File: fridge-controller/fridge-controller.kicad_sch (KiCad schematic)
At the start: 11 parts, among them M1 Fan, U2 AMS1117-5.0, U3 Arduino_Pro_Mini, U4 TLP127, U5 Secop BD35F

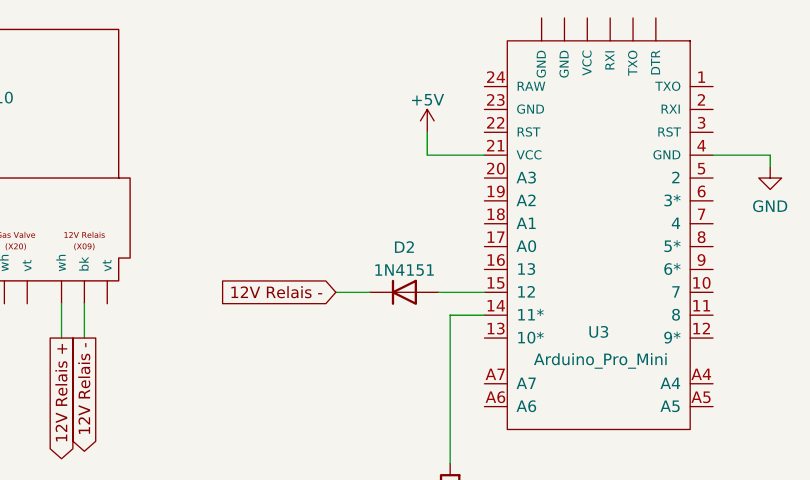
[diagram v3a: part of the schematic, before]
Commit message: Updated fridge-controller
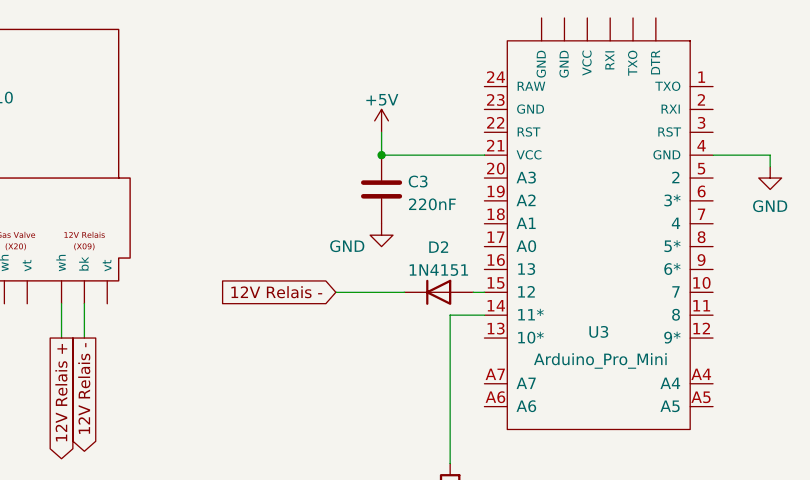
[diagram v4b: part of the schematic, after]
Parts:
- added C3: 220nF, symbol Device:C
- gave numbers to parts that had none: 1
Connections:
- net +5V: now also C3.1
- net GND: now also C3.2
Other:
- moved on the sheet: D2
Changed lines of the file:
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@@
   (title_block
     (title "Secop BD35F Compressor Speed Controller")
-    (date "2025-02-14")
+    (date "2025-02-16")
     (company "Copyright (C) 2025, Karim Hraibi")
     (comment 1 "Enables variable speed control over 5 kHz PWM signal.")
@@
   (junction (at 85.09 90.17) (diameter 0) (color 0 0 0 0)
   )
+  (junction (at 86.36 34.29) (diameter 0) (color 0 0 0 0)
+  )
   (wire (pts (xy 152.4 80.01) (xy 154.94 80.01))
     (stroke (width 0) (type default) (color 0 0 0 0))
@@
     (stroke (width 0) (type default) (color 0 0 0 0))
   )
-  (wire (pts (xy 97.79 49.53) (xy 92.71 49.53))
+  (wire (pts (xy 97.79 49.53) (xy 96.52 49.53))
     (stroke (width 0) (type default) (color 0 0 0 0))
   )
@@
     (stroke (width 0) (type default) (color 0 0 0 0))
   )
-  (wire (pts (xy 91.44 34.29) (xy 97.79 34.29))
+  (wire (pts (xy 86.36 34.29) (xy 97.79 34.29))
     (stroke (width 0) (type default) (color 0 0 0 0))
   )
@@
     (stroke (width 0) (type default) (color 0 0 0 0))
   )
-  (wire (pts (xy 85.09 49.53) (xy 81.28 49.53))
+  (wire (pts (xy 88.9 49.53) (xy 81.28 49.53))
     (stroke (width 0) (type default) (color 0 0 0 0))
   )
@@
     (stroke (width 0) (type default) (color 0 0 0 0))
   )
-  (wire (pts (xy 91.44 31.75) (xy 91.44 34.29))
+  (wire (pts (xy 86.36 31.75) (xy 86.36 34.29))
     (stroke (width 0) (type default) (color 0 0 0 0))
   )
@@
     )
   )
+  (symbol (lib_id "Device:C") (at 86.36 38.1 0) (unit 1)
+    (in_bom yes) (on_board yes)
+    (property "Reference" "C3" (id 0) (at 89.281 37.2653 0)
+      (effects (font (size 1.27 1.27)) (justify left))
+    )
+    (property "Value" "220nF" (id 1) (at 89.281 39.8022 0)
+      (effects (font (size 1.27 1.27)) (justify left))
+    )
+    (property "Footprint" "" (id 2) (at 87.3252 41.91 0)
+      (effects (font (size 1.27 1.27)) hide)
+    )
+    (property "Datasheet" "~" (id 3) (at 86.36 38.1 0)
+      (effects (font (size 1.27 1.27)) hide)
+    )
+    (pin "1")
+    (pin "2")
+  )
   (symbol (lib_id "Device:R") (at 93.98 72.39 180) (unit 1)
     (in_bom yes) (on_board yes) (fields_autoplaced)
@@
   (symbol (lib_id "power:GND") (at 100.33 87.63 0) (unit 1)
     (in_bom yes) (on_board yes) (fields_autoplaced)
-    (property "Reference" "#PWR04" (id 0) (at 100.33 93.98 0)
+    (property "Reference" "#PWR05" (id 0) (at 100.33 93.98 0)
       (effects (font (size 1.27 1.27)) hide)
     )
@@
     (pin "1")
   )
-  (symbol (lib_id "Diode:1N4151") (at 88.9 49.53 0) (unit 1)
-    (in_bom yes) (on_board yes) (fields_autoplaced)
-    (property "Reference" "D2" (id 0) (at 88.9 44.5602 0))
-    (property "Value" "1N4151" (id 1) (at 88.9 47.0971 0))
-    (property "Footprint" "Diode_THT:D_DO-35_SOD27_P7.62mm_Horizontal" (id 2) (at 88.9 53.975 0)
-      (effects (font (size 1.27 1.27)) hide)
-    )
-    (property "Datasheet" "http://www.microsemi.com/document-portal/doc_view/11580-lds-0239" (id 3) (at 88.9 49.53 0)
+  (symbol (lib_id "Diode:1N4151") (at 92.71 49.53 0) (unit 1)
+    (in_bom yes) (on_board yes) (fields_autoplaced)
+    (property "Reference" "D2" (id 0) (at 92.71 44.5602 0))
+    (property "Value" "1N4151" (id 1) (at 92.71 47.0971 0))
+    (property "Footprint" "Diode_THT:D_DO-35_SOD27_P7.62mm_Horizontal" (id 2) (at 92.71 53.975 0)
+      (effects (font (size 1.27 1.27)) hide)
+    )
+    (property "Datasheet" "http://www.microsemi.com/document-portal/doc_view/11580-lds-0239" (id 3) (at 92.71 49.53 0)
       (effects (font (size 1.27 1.27)) hide)
     )
@@
   (symbol (lib_id "power:GND") (at 129.54 35.56 0) (unit 1)
     (in_bom yes) (on_board yes) (fields_autoplaced)
-    (property "Reference" "#PWR05" (id 0) (at 129.54 41.91 0)
+    (property "Reference" "#PWR06" (id 0) (at 129.54 41.91 0)
       (effects (font (size 1.27 1.27)) hide)
     )
@@
     (pin "1")
   )
-  (symbol (lib_id "power:+5V") (at 91.44 31.75 0) (unit 1)
-    (in_bom yes) (on_board yes) (fields_autoplaced)
-    (property "Reference" "#PWR03" (id 0) (at 91.44 35.56 0)
-      (effects (font (size 1.27 1.27)) hide)
-    )
-    (property "Value" "+5V" (id 1) (at 91.44 28.1742 0))
-    (property "Footprint" "" (id 2) (at 91.44 31.75 0)
-      (effects (font (size 1.27 1.27)) hide)
-    )
-    (property "Datasheet" "" (id 3) (at 91.44 31.75 0)
+  (symbol (lib_id "power:+5V") (at 86.36 31.75 0) (unit 1)
+    (in_bom yes) (on_board yes) (fields_autoplaced)
+    (property "Reference" "#PWR03" (id 0) (at 86.36 35.56 0)
+      (effects (font (size 1.27 1.27)) hide)
+    )
+    (property "Value" "+5V" (id 1) (at 86.36 28.1742 0))
+    (property "Footprint" "" (id 2) (at 86.36 31.75 0)
+      (effects (font (size 1.27 1.27)) hide)
+    )
+    (property "Datasheet" "" (id 3) (at 86.36 31.75 0)
       (effects (font (size 1.27 1.27)) hide)
     )
@@
     (pin "1")
     (pin "2")
+  )
+  (symbol (lib_id "power:GND") (at 86.36 41.91 0) (unit 1)
+    (in_bom yes) (on_board yes)
+    (property "Reference" "#PWR04" (id 0) (at 86.36 48.26 0)
+      (effects (font (size 1.27 1.27)) hide)
+    )
+    (property "Value" "GND" (id 1) (at 82.55 44.45 0))
+    (property "Footprint" "" (id 2) (at 86.36 41.91 0)
+      (effects (font (size 1.27 1.27)) hide)
+    )
+    (property "Datasheet" "" (id 3) (at 86.36 41.91 0)
+      (effects (font (size 1.27 1.27)) hide)
+    )
+    (pin "1")
   )
   (symbol (lib_id "Device:C_Polarized") (at 85.09 85.09 0) (unit 1)
@@
   (symbol (lib_id "microfarad-de:Dometic RML10") (at 36.83 36.83 0) (unit 1)
     (in_bom yes) (on_board yes)
-    (property "Reference" "U?" (id 0) (at 36.83 27.94 0)
+    (property "Reference" "U1" (id 0) (at 36.83 27.94 0)
       (effects (font (size 1.27 1.27)) hide)
     )
@@
       (reference "#PWR03") (unit 1) (value "+5V") (footprint "")
     )
+    (path "/abe14503-b46e-489b-a495-0c3d25945e8c"
+      (reference "#PWR04") (unit 1) (value "GND") (footprint "")
+    )
     (path "/3c326e87-7507-4b25-8c53-00417351d764"
-      (reference "#PWR04") (unit 1) (value "GND") (footprint "")
+      (reference "#PWR05") (unit 1) (value "GND") (footprint "")
     )
     (path "/9d7f950d-b8e8-43c9-b5a7-b9b359cf80da"
-      (reference "#PWR05") (unit 1) (value "GND") (footprint "")
+      (reference "#PWR06") (unit 1) (value "GND") (footprint "")
     )
     (path "/92230a79-171b-45cd-b9aa-e7c169691012"
@@
       (reference "C2") (unit 1) (value "10µF") (footprint "")
     )
+    (path "/0f25ba74-7a0e-43b6-a3da-0d8a5456083d"
+      (reference "C3") (unit 1) (value "220nF") (footprint "")
+    )
     (path "/aa01f852-ed39-42ba-a280-6b5ee5c376e5"
       (reference "D1") (unit 1) (value "1N4151") (footprint "Diode_THT:D_DO-35_SOD27_P7.62mm_Horizontal")
@@
       (reference "R1") (unit 1) (value "470Ω") (footprint "")
     )
+    (path "/f34b6659-deac-4243-935d-e65feaddf571"
+      (reference "U1") (unit 1) (value "Dometic RML10") (footprint "")
+    )
     (path "/b8b41635-00c1-442e-ba06-4137bff20311"
       (reference "U2") (unit 1) (value "AMS1117-5.0") (footprint "Package_TO_SOT_SMD:SOT-223-3_TabPin2")
@@
       (reference "U5") (unit 1) (value "Secop BD35F") (footprint "")
     )
-    (path "/f34b6659-deac-4243-935d-e65feaddf571"
-      (reference "U?") (unit 1) (value "Dometic RML10") (footprint "")
-    )
-  )
+  )

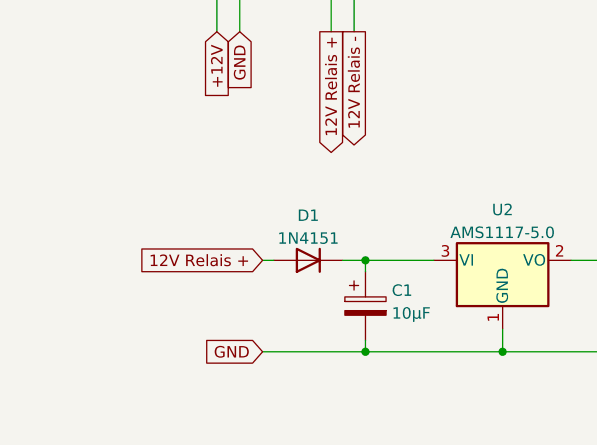
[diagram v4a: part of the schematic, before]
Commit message: Updated fridge-controller
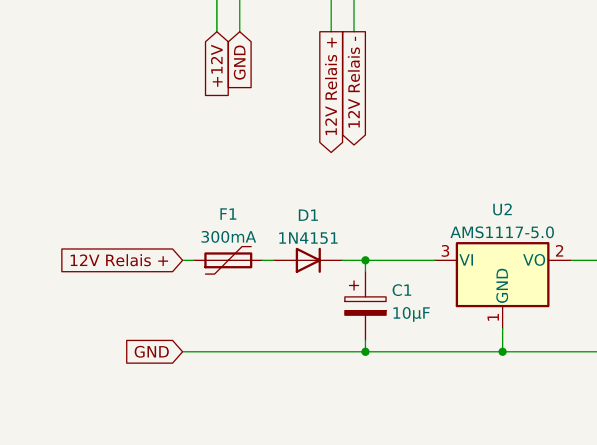
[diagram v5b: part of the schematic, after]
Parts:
- added F1: 300mA, symbol Device:Polyfuse
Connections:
- net 12V Relais +: now also F1.1; no longer D1.2 (A)
- new net: D1.2 (A), F1.2
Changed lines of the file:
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@@
   (title_block
     (title "Secop BD35F Compressor Speed Controller")
-    (date "2025-02-16")
+    (date "2025-02-20")
     (company "Copyright (C) 2025, Karim Hraibi")
     (comment 1 "Enables variable speed control over 5 kHz PWM signal.")
@@
     (stroke (width 0) (type default) (color 0 0 0 0))
   )
-  (wire (pts (xy 43.18 90.17) (xy 54.61 90.17))
+  (wire (pts (xy 34.29 90.17) (xy 54.61 90.17))
     (stroke (width 0) (type default) (color 0 0 0 0))
   )
@@
   )
   (wire (pts (xy 85.09 90.17) (xy 85.09 92.71))
+    (stroke (width 0) (type default) (color 0 0 0 0))
+  )
+  (wire (pts (xy 34.29 80.01) (xy 35.56 80.01))
     (stroke (width 0) (type default) (color 0 0 0 0))
   )
@@
     )
   )
-  (global_label "12V Relais +" (shape input) (at 43.18 80.01 180) (fields_autoplaced)
-    (effects (font (size 1.27 1.27)) (justify right))
-    (property "Intersheet References" "${INTERSHEET_REFS}" (id 0) (at 27.9459 79.9306 0)
+  (global_label "12V Relais +" (shape input) (at 34.29 80.01 180) (fields_autoplaced)
+    (effects (font (size 1.27 1.27)) (justify right))
+    (property "Intersheet References" "${INTERSHEET_REFS}" (id 0) (at 19.0559 79.9306 0)
       (effects (font (size 1.27 1.27)) (justify right) hide)
     )
@@
     )
   )
-  (global_label "GND" (shape input) (at 43.18 90.17 180) (fields_autoplaced)
-    (effects (font (size 1.27 1.27)) (justify right))
-    (property "Intersheet References" "${INTERSHEET_REFS}" (id 0) (at 36.8964 90.0906 0)
+  (global_label "GND" (shape input) (at 34.29 90.17 180) (fields_autoplaced)
+    (effects (font (size 1.27 1.27)) (justify right))
+    (property "Intersheet References" "${INTERSHEET_REFS}" (id 0) (at 28.0064 90.0906 0)
       (effects (font (size 1.27 1.27)) (justify right) hide)
     )
@@
     )
     (property "Datasheet" "~" (id 3) (at 93.98 72.39 0)
+      (effects (font (size 1.27 1.27)) hide)
+    )
+    (pin "1")
+    (pin "2")
+  )
+  (symbol (lib_id "Device:Polyfuse") (at 39.37 80.01 90) (unit 1)
+    (in_bom yes) (on_board yes) (fields_autoplaced)
+    (property "Reference" "F1" (id 0) (at 39.37 74.9132 90))
+    (property "Value" "300mA" (id 1) (at 39.37 77.4501 90))
+    (property "Footprint" "" (id 2) (at 44.45 78.74 0)
+      (effects (font (size 1.27 1.27)) (justify left) hide)
+    )
+    (property "Datasheet" "~" (id 3) (at 39.37 80.01 0)
       (effects (font (size 1.27 1.27)) hide)
     )
@@
       (reference "D2") (unit 1) (value "1N4151") (footprint "Diode_THT:D_DO-35_SOD27_P7.62mm_Horizontal")
     )
+    (path "/3a6d5aaa-665c-466e-bcde-bdc9979592ea"
+      (reference "F1") (unit 1) (value "300mA") (footprint "")
+    )
     (path "/bbc08eff-8189-4e3a-8f41-42391d94c336"

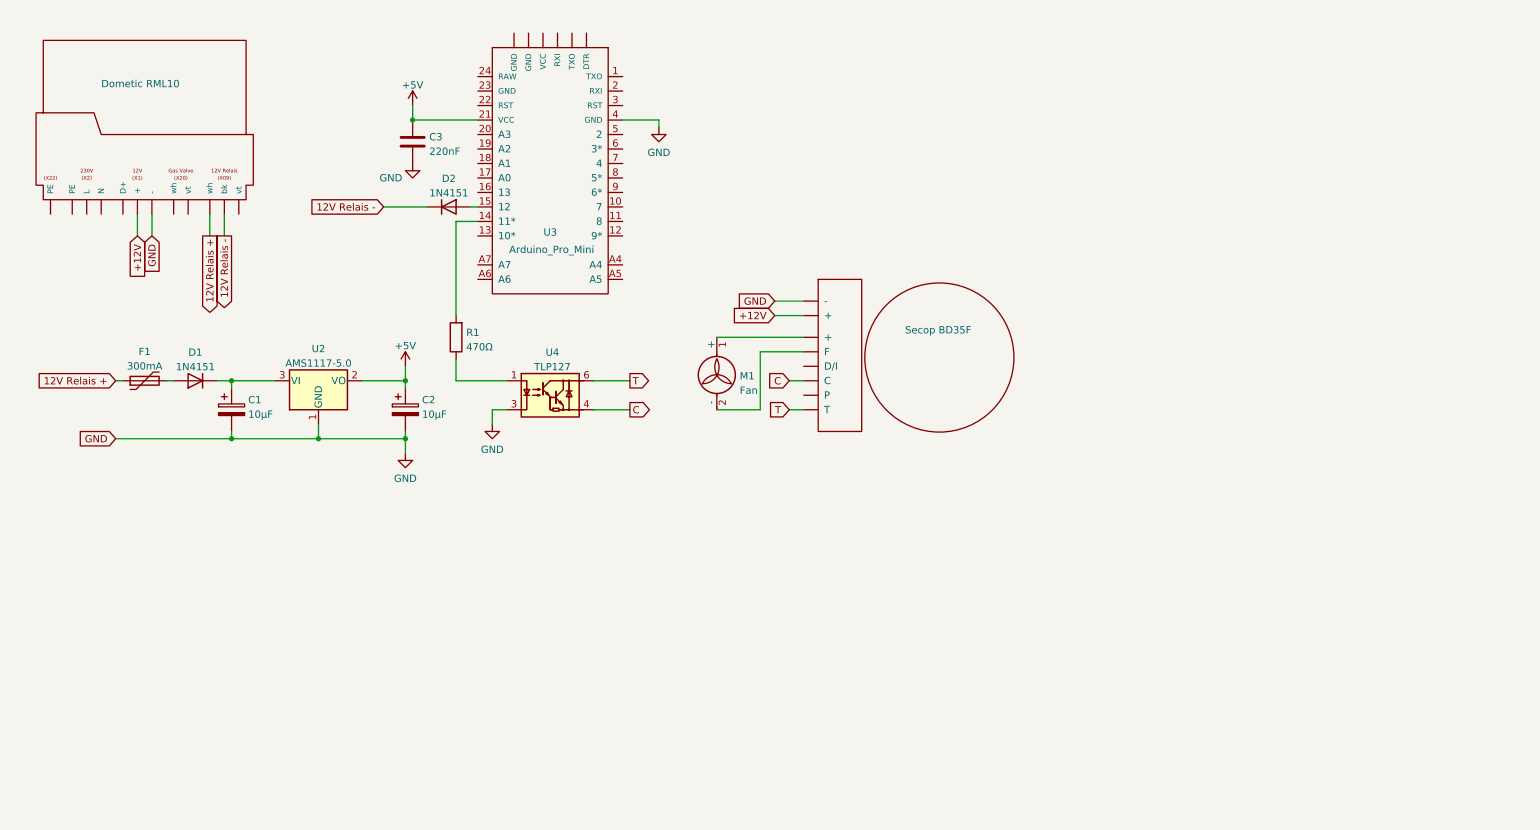
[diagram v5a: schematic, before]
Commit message: Updated fridge-controller
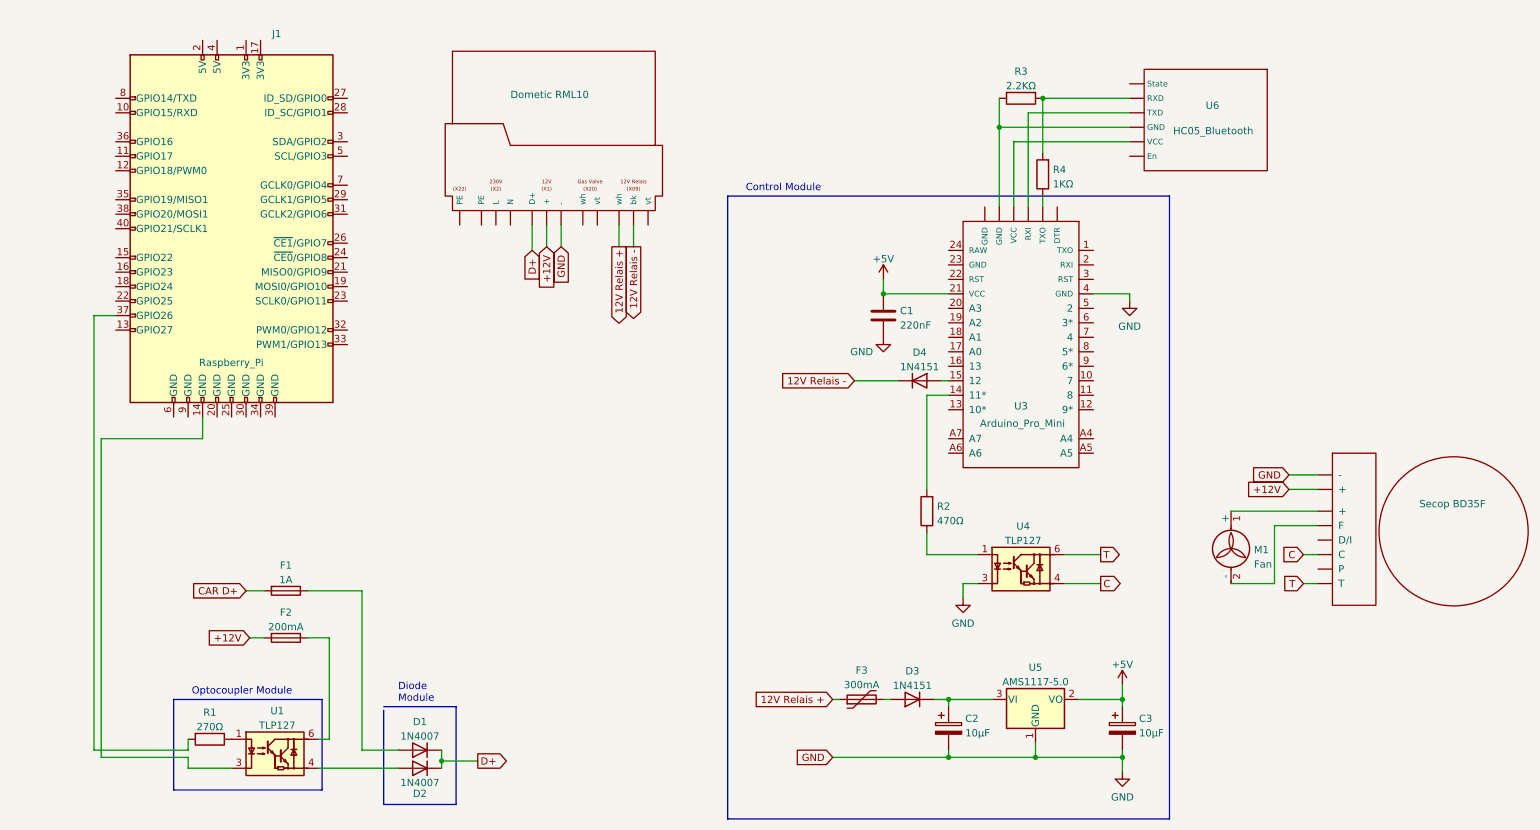
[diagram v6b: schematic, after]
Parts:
- added D1, D2: 1N4007, Diode_THT:D_DO-41_SOD81_P10.16mm_Horizontal, symbol Diode:1N4007
- added F1: 1A, symbol Device:Fuse
- added F2: 200mA, symbol Device:Fuse
- added J1: Raspberry_Pi, symbol Connector:Raspberry_Pi_2_3
- added R1: 270Ω, symbol Device:R
- added R3: 2.2KΩ, symbol Device:R
- added R4: 1KΩ, symbol Device:R
- added U1: TLP127, Package_SO:MFSOP6-4_4.4x3.6mm_P1.27mm, symbol Isolator:TLP127
- added U6: HC05_Bluetooth, symbol microfarad-de:HC05_Bluetooth
- renumbered C3 to C1, C1 to C2, C2 to C3, D1 to D3, D2 to D4, F1 to F3, R1 to R2, U1 to U2, U2 to U5, U5 to U7
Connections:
- net +12V: now also F2.2
- new net: F2.1, U1.6
- new net: D1.2 (A), F1.1
- new net: J1.14 (GND), U1.3
- new net: J1.37 (GPIO26), R1.2
- new net: R1.1, U1.1
- new net: D2.2 (A), U1.4
- new net: R3.1, R4.2, U6. (VCC)
- new net: R3.2, U3. (VCC), U6. (VCC)
- new net: U3. (VCC), U6. (VCC) (x2)
- new net: R4.1, U3. (VCC)
- new net CAR D+: F1.2
- new net D+: D1.1 (K), D2.1 (K), U2. (wh)
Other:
- note added: "Control Module"
- note added: "Diode Module"
- note added: "Optocoupler Module"
- moved on the sheet: C1, C2, C3, D3, D4, F3, M1, R2, U3, U4, U5

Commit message: Updated fridge controller
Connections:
- net at J1.14 (GND): no longer U1.3
- net at J1.39 (GND): now also U1.3
- net at U6. (VCC): now also U3. (VCC)
- net at U3. (VCC): no longer U6. (VCC)
- new net: R3.2, U3. (VCC), U6. (VCC)
- new net: U3. (VCC), U6. (VCC)
- now unconnected: U3. (VCC), U3. (VCC)
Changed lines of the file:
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@@
     (stroke (width 0) (type default) (color 0 0 0 0))
   )
-  (wire (pts (xy 49.53 90.17) (xy 31.75 90.17))
+  (wire (pts (xy 31.75 90.17) (xy 62.23 90.17))
     (stroke (width 0) (type default) (color 0 0 0 0))
   )
@@
     (stroke (width 0) (type default) (color 0 0 0 0))
   )
+  (wire (pts (xy 62.23 90.17) (xy 62.23 86.36))
+    (stroke (width 0) (type default) (color 0 0 0 0))
+  )
   (wire (pts (xy 160.02 135.89) (xy 161.29 135.89))
     (stroke (width 0) (type default) (color 0 0 0 0))
@@
     (stroke (width 0) (type default) (color 0 0 0 0))
   )
-  (wire (pts (xy 49.53 86.36) (xy 49.53 90.17))
-    (stroke (width 0) (type default) (color 0 0 0 0))
-  )
